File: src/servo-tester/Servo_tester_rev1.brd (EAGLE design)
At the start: 79.7 x 41.9 mm, 23 parts, among them IC1 7806T

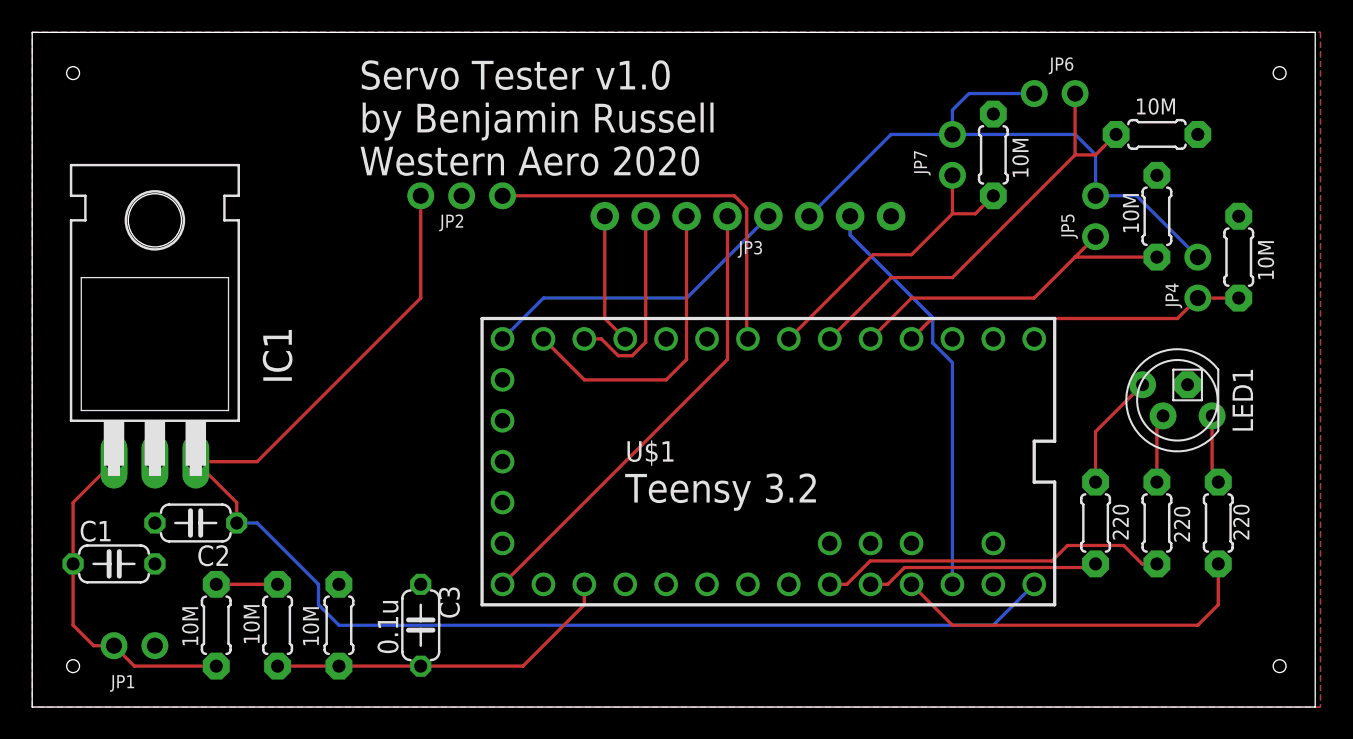
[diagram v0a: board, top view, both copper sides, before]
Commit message: Moved led to unblock usb port, tidied up buttons
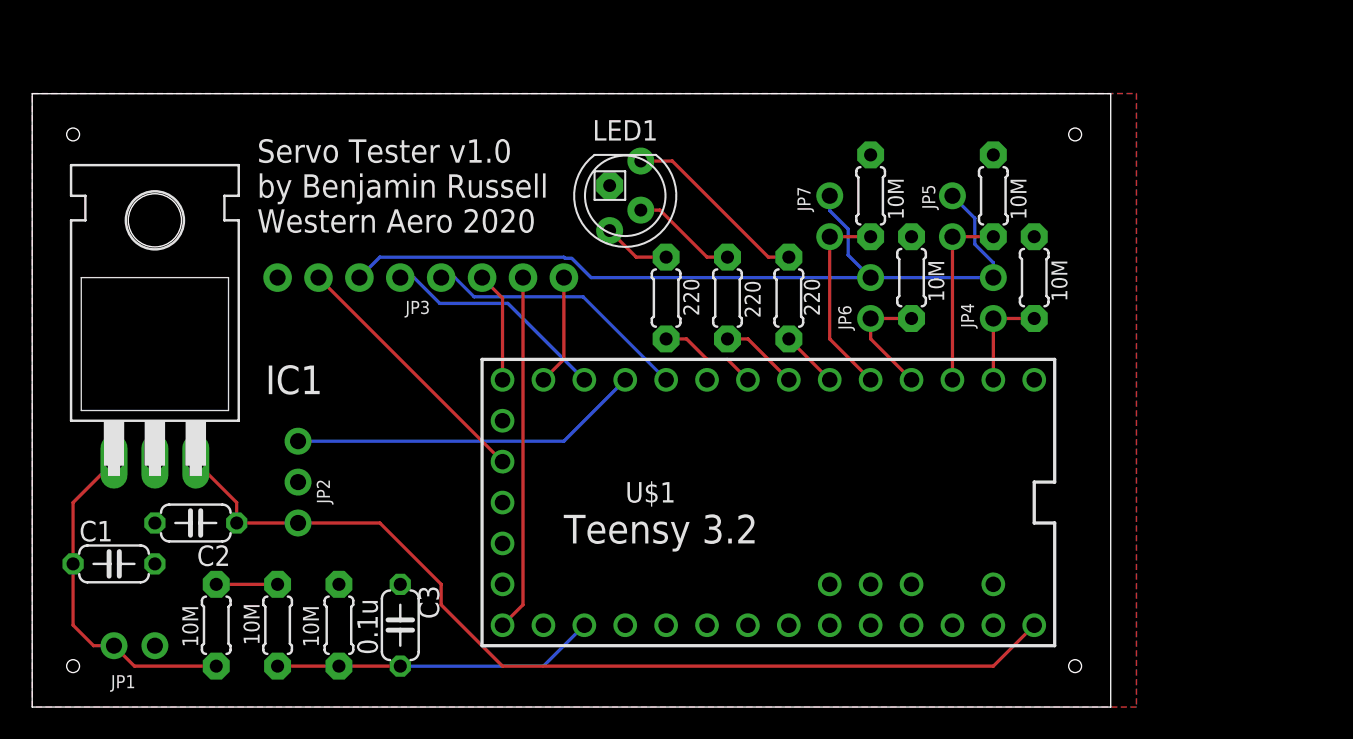
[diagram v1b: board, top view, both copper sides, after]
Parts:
- moved LED1 36.6 mm to (43.2, 31.8), turned to 270 degrees
- moved R4 30.1 mm to (45.7, 25.4)
- moved R5 30.1 mm to (49.5, 25.4)
- moved R6 30.1 mm to (53.3, 25.4)
- moved JP3 20.7 mm to (30.5, 26.7), turned to 180 degrees
- moved JP2 20.5 mm to (22.9, 14.0), turned to 90 degrees
- moved R9 17.6 mm to (61.0, 26.7), turned to 270 degrees
- moved JP6 17.1 mm to (58.4, 25.4), turned to 90 degrees
- moved R7 12.8 mm to (68.6, 26.7)
- moved JP4 12.8 mm to (66.0, 25.4)
- moved R8 10.2 mm to (66.0, 31.8)
- moved JP5 8.89 mm to (63.5, 30.5)
- moved JP7 8.52 mm to (55.9, 30.5)
- moved R10 8.03 mm to (58.4, 31.8)
- moved U$1 2.54 mm to (52.1, 12.7)
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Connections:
- net BTN1: now also U$1.0; no longer U$1.2
- net BTN2: now also U$1.1; no longer U$1.3
- net BTN3: now also U$1.2; no longer U$1.4
- net BTN4: now also U$1.3; no longer U$1.5
- net LEDB: now also U$1.6; no longer U$1.22/A8
- net LEDG: now also U$1.5; no longer U$1.21/A7
- net LEDR: now also U$1.4; no longer U$1.23/A9
- net SCREEN_CLK: now also U$1.13; no longer U$1.10
- net SCREEN_CS: now also U$1.10; no longer U$1.12
- net SCREEN_DATA: now also U$1.11; no longer U$1.9
- net SCREEN_DC: now also U$1.12; no longer U$1.11
- net SCREEN_RST: now also U$1.8; no longer U$1.13
- net SERVO: now also U$1.9; no longer U$1.6
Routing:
- net 6V: track 83.3 -> 59.9 mm
- net LEDR: track 23.2 -> 3.59 mm
- net BTN3: track 26.9 -> 7.40 mm
- net LEDG: track 21.8 -> 4.86 mm
- net BTN1: track 21.4 -> 6.35 mm
- net 33V_PULLUP: track 37.9 -> 52.7 mm
- net SCREEN_DC: track 19.4 -> 6.88 mm
- net SCREEN_RST: track 28.6 -> 16.6 mm
- net BTN2: track 21.7 -> 11.4 mm
- net SCREEN_CLK: track 12.4 -> 22.1 mm
- net 33V: track 25.5 -> 16.2 mm
- net LEDB: track 14.5 -> 6.13 mm
- net N$13: track 4.27 -> 11.7 mm
- net BTN4: track 18.8 -> 12.5 mm
- net SCREEN_CS: track 19.7 -> 14.1 mm
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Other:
- board size 79.7 x 41.9 mm -> 67 x 38.1 mm
